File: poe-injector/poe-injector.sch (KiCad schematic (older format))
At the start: 34 parts, among them IC1 ATTINY44-SS, J1 AVRISP6, Q1 ZXMP10A17E6, Q2 2N7002K, Q3 ZXMP10A17E6, Q4 2N7002K, U2 LTC6101, U4 LTC6101

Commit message: Add Gerbers, and prepare things for manufacture some more
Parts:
- added C1: 10u, symbol C
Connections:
- net +5V: now also C1.1
- net GND: now also C1.2
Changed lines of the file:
@@
-EESchema Schematic File Version 2  date 2/5/2013 5:40:43 PM
+EESchema Schematic File Version 2  date 2/5/2013 10:25:32 PM
 LIBS:power
 LIBS:device
@@
 Sheet 1 1
 Title ""
-Date "5 feb 2013"
+Date "6 feb 2013"
 Rev ""
 Comp ""
@@
 $EndDescr
 $Comp
+L +5V #PWR01
+U 1 1 5111AFF4
+P 3600 1850
+F 0 "#PWR01" H 3600 1940 20  0001 C CNN
+F 1 "+5V" H 3600 1940 30  0000 C CNN
+	1    3600 1850
+	1    0    0    -1
+$EndComp
+$Comp
+L GND #PWR02
+U 1 1 5111AFED
+P 3600 2250
+F 0 "#PWR02" H 3600 2250 30  0001 C CNN
+F 1 "GND" H 3600 2180 30  0001 C CNN
+	1    3600 2250
+	1    0    0    -1
+$EndComp
+$Comp
+L C C1
+U 1 1 5111AFE5
+P 3600 2050
+F 0 "C1" H 3650 2150 50  0000 L CNN
+F 1 "10u" H 3650 1950 50  0000 L CNN
+	1    3600 2050
+	1    0    0    -1
+$EndComp
+$Comp
 L VPP #PWR19
 U 1 1 511185E5
@@
 $EndComp
 $Comp
-L +48V #PWR01
+L +48V #PWR03
 U 1 1 511185CE
 P 9450 1300
-F 0 "#PWR01" H 9450 1430 20  0001 C CNN
+F 0 "#PWR03" H 9450 1430 20  0001 C CNN
 F 1 "+48V" H 9450 1400 30  0000 C CNN
 	1    9450 1300
@@
 	4150 3650 3600 3650
 $Comp
-L +48V #PWR02
+L +48V #PWR04
 U 1 1 5111849B
 P 7550 5050
-F 0 "#PWR02" H 7550 5180 20  0001 C CNN
+F 0 "#PWR04" H 7550 5180 20  0001 C CNN
 F 1 "+48V" H 7550 5150 30  0000 C CNN
 	1    7550 5050
@@
 $EndComp
 $Comp
-L +48V #PWR03
+L +48V #PWR05
 U 1 1 51118493
 P 7100 2700
-F 0 "#PWR03" H 7100 2830 20  0001 C CNN
+F 0 "#PWR05" H 7100 2830 20  0001 C CNN
 F 1 "+48V" H 7100 2800 30  0000 C CNN
 	1    7100 2700
@@
 $EndComp
 $Comp
-L +48V #PWR04
+L +48V #PWR06
 U 1 1 51118467
 P 8700 1250
-F 0 "#PWR04" H 8700 1380 20  0001 C CNN
+F 0 "#PWR06" H 8700 1380 20  0001 C CNN
 F 1 "+48V" H 8700 1350 30  0000 C CNN
 	1    8700 1250
@@
 $EndComp
 $Comp
-L GND #PWR05
+L GND #PWR07
 U 1 1 511182B8
 P 5900 7550
-F 0 "#PWR05" H 5900 7550 30  0001 C CNN
+F 0 "#PWR07" H 5900 7550 30  0001 C CNN
 F 1 "GND" H 5900 7480 30  0001 C CNN
 	1    5900 7550
@@
 $EndComp
 $Comp
-L GND #PWR06
+L GND #PWR08
 U 1 1 51118117
 P 9450 2300
-F 0 "#PWR06" H 9450 2300 30  0001 C CNN
+F 0 "#PWR08" H 9450 2300 30  0001 C CNN
 F 1 "GND" H 9450 2230 30  0001 C CNN
 	1    9450 2300
@@
 $EndComp
 $Comp
-L GND #PWR07
+L GND #PWR09
 U 1 1 51117B98
 P 1500 4550
-F 0 "#PWR07" H 1500 4550 30  0001 C CNN
+F 0 "#PWR09" H 1500 4550 30  0001 C CNN
 F 1 "GND" H 1500 4480 30  0001 C CNN
 	1    1500 4550
@@
 $EndComp
 $Comp
-L +5V #PWR08
+L +5V #PWR010
 U 1 1 51117B3E
 P 1500 3350
-F 0 "#PWR08" H 1500 3440 20  0001 C CNN
+F 0 "#PWR010" H 1500 3440 20  0001 C CNN
 F 1 "+5V" H 1500 3440 30  0000 C CNN
 	1    1500 3350
@@
 $EndComp
 $Comp
-L GND #PWR09
+L GND #PWR011
 U 1 1 5111744B
 P 8300 2700
-F 0 "#PWR09" H 8300 2700 30  0001 C CNN
+F 0 "#PWR011" H 8300 2700 30  0001 C CNN
 F 1 "GND" H 8300 2630 30  0001 C CNN
 	1    8300 2700
@@
 $EndComp
 $Comp
-L GND #PWR010
+L GND #PWR012
 U 1 1 51117447
 P 8750 5050
-F 0 "#PWR010" H 8750 5050 30  0001 C CNN
+F 0 "#PWR012" H 8750 5050 30  0001 C CNN
 F 1 "GND" H 8750 4980 30  0001 C CNN
 	1    8750 5050
@@
 $EndComp
 $Comp
-L GND #PWR011
+L GND #PWR013
 U 1 1 511083A8
 P 4900 1850
-F 0 "#PWR011" H 4900 1850 30  0001 C CNN
+F 0 "#PWR013" H 4900 1850 30  0001 C CNN
 F 1 "GND" H 4900 1780 30  0001 C CNN
 	1    4900 1850
@@
 $EndComp
 $Comp
-L GND #PWR012
+L GND #PWR014
 U 1 1 5110833F
 P 5200 4800
-F 0 "#PWR012" H 5200 4800 30  0001 C CNN
+F 0 "#PWR014" H 5200 4800 30  0001 C CNN
 F 1 "GND" H 5200 4730 30  0001 C CNN
 	1    5200 4800
@@
 $EndComp
 $Comp
-L +48V #PWR013
+L +48V #PWR015
 U 1 1 51106F2B
 P 8800 3600
-F 0 "#PWR013" H 8800 3730 20  0001 C CNN
+F 0 "#PWR015" H 8800 3730 20  0001 C CNN
 F 1 "+48V" H 8800 3700 30  0000 C CNN
 	1    8800 3600
@@
 $EndComp
 $Comp
-L GND #PWR014
+L GND #PWR016
 U 1 1 51105C25
 P 4900 2450
-F 0 "#PWR014" H 4900 2450 30  0001 C CNN
+F 0 "#PWR016" H 4900 2450 30  0001 C CNN
 F 1 "GND" H 4900 2380 30  0001 C CNN
 	1    4900 2450
@@
 P 5350 2200
 F 0 "EOUT2" V 5300 2200 60  0000 C CNN
-F 1 "CONN_10" V 5400 2200 60  0000 C CNN
+F 1 "CONN_10" V 5400 2200 60  0001 C CNN
 	1    5350 2200
 	0    1    1    0
@@
 P 5350 2800
 F 0 "EIN2" V 5300 2800 60  0000 C CNN
-F 1 "CONN_10" V 5400 2800 60  0000 C CNN
+F 1 "CONN_10" V 5400 2800 60  0001 C CNN
 	1    5350 2800
 	0    1    1    0
 $EndComp
 $Comp
-L GND #PWR015
+L GND #PWR017
 U 1 1 51105BDE
 P 5200 4200
-F 0 "#PWR015" H 5200 4200 30  0001 C CNN
+F 0 "#PWR017" H 5200 4200 30  0001 C CNN
 F 1 "GND" H 5200 4130 30  0001 C CNN
 	1    5200 4200
@@
 $EndComp
 $Comp
-L GND #PWR016
+L GND #PWR018
 U 1 1 510E9A8D
 P 1100 1350
-F 0 "#PWR016" H 1100 1350 30  0001 C CNN
+F 0 "#PWR018" H 1100 1350 30  0001 C CNN
 F 1 "GND" H 1100 1280 30  0001 C CNN
 	1    1100 1350
@@
 $EndComp
 $Comp
-L +5V #PWR017
+L +5V #PWR019
 U 1 1 510E9A89
 P 900 1350
-F 0 "#PWR017" H 900 1440 20  0001 C CNN
+F 0 "#PWR019" H 900 1440 20  0001 C CNN
 F 1 "+5V" H 900 1440 30  0000 C CNN
 	1    900  1350
@@
 P 6400 2450
 F 0 "Q2" H 6400 2550 60  0000 C CNN
-F 1 "2N7002K" H 6400 2450 60  0000 C CNN
+F 1 "2N7002K" H 6400 2450 60  0001 C CNN
 	1    6400 2450
 	1    0    0    -1

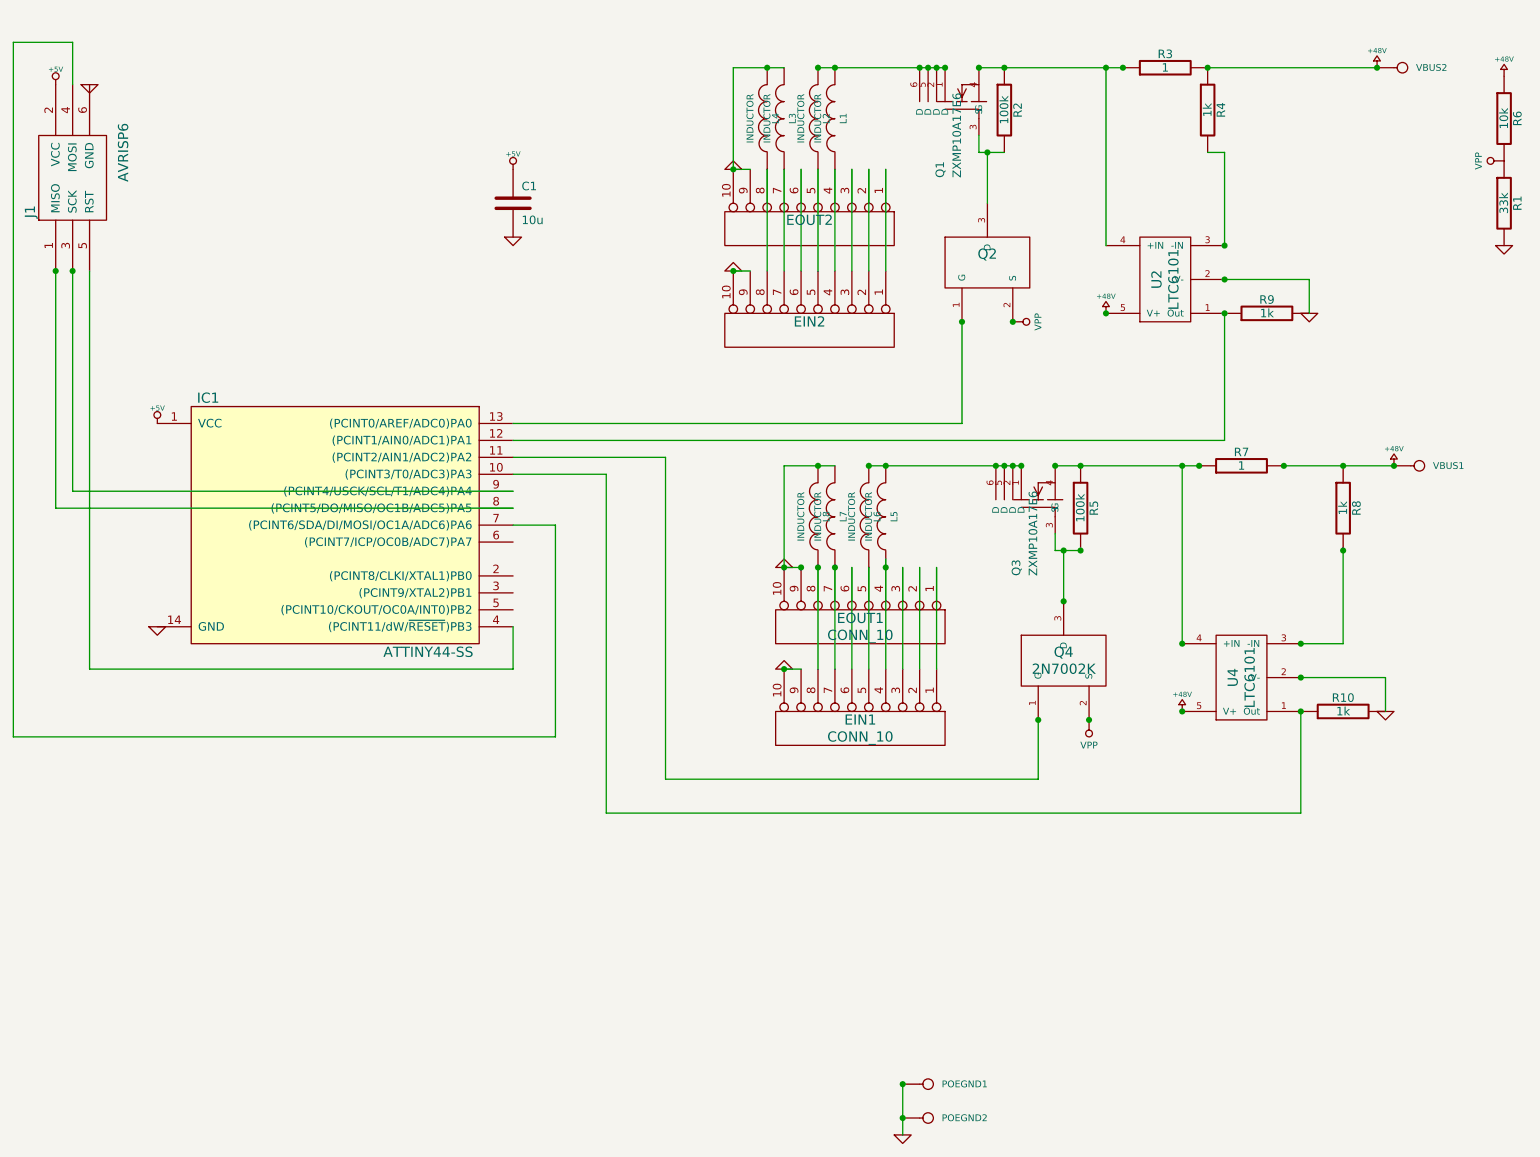
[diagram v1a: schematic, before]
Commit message: Possible trouble in paradise: how to detect PoE ready?
Added 3 resistors to pull the ADC in appropriate directions: towards +5,
towards ground, and towards the Ethernet leg.  The last will be either:
+48V: PoE is sending power, ADC gets 4.36V plus a little pull-up from
the +5V resistor.  As long as it's not more than 5V, whatever.
25k resistance to ground (PoE ready but not on yet): ADC gets 1.17V.
Open circuit (Not PoE ready): ADC gets 4.78V.
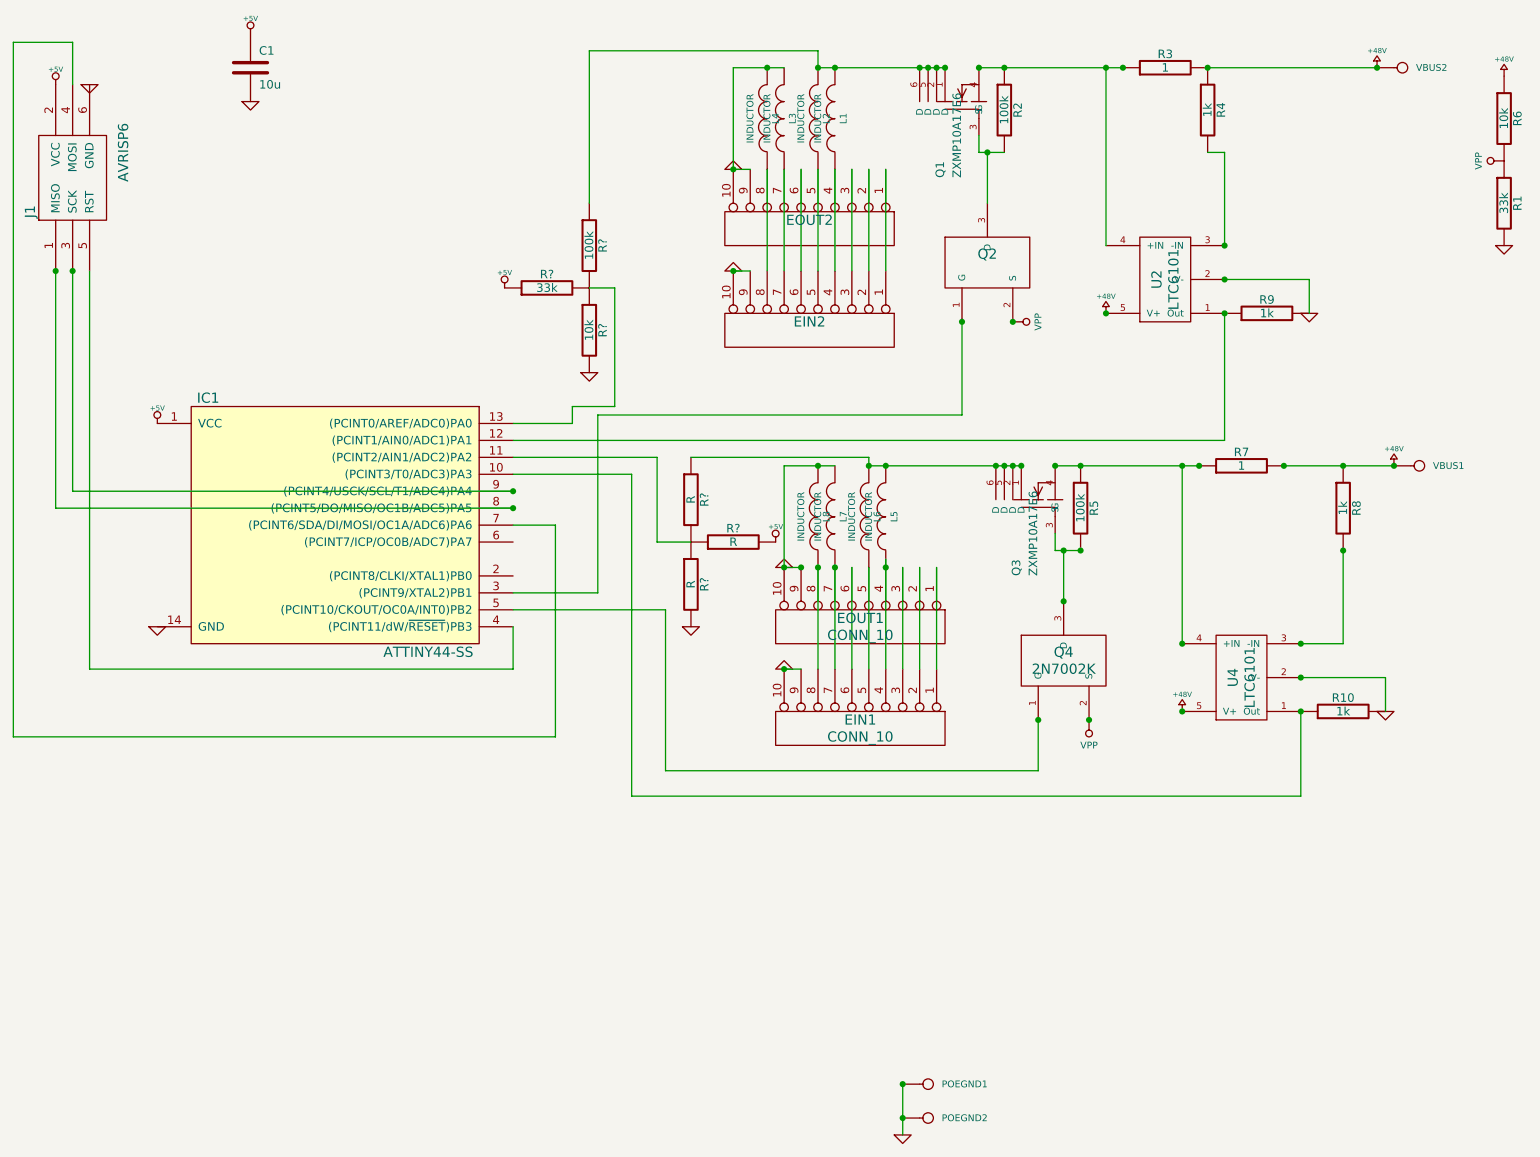
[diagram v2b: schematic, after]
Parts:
- added R?: 10k, symbol R
- added R?: 100k, symbol R
- added R?: 33k, symbol R
- added R? (x3): R, symbol R
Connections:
- net +5V: now also R?.1, R?.2
- net GND: now also R?.2, R?.2
- net at L1.2, L2.2, Q1.1 (D)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: now also R?.1
- net at Q2.1 (G): now also IC1.3 ((PCINT9/XTAL2)PB1); no longer IC1.13 ((PCINT0/AREF/ADC0)PA0)
- net at Q4.1 (G): now also IC1.5 ((PCINT10/CKOUT/OC0A/INT0)PB2); no longer IC1.11 ((PCINT2/AIN1/ADC2)PA2)
- net at L5.2, L6.2, Q3.1 (D)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: now also R?.1
- new net: IC1.11 ((PCINT2/AIN1/ADC2)PA2), R?.1, R?.1, R?.2
- new net: IC1.13 ((PCINT0/AREF/ADC0)PA0), R?.1, R?.2, R?.2
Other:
- moved on the sheet: C1
